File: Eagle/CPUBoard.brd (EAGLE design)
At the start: 100 x 80 mm, 33 parts, among them IC2 MAX232, IC3 MAX485CPA, J1 DISPLAY, J2 BUTTON_BOARD, J3 RELAY_BOARD, Q1 12.000MHz, X6 MKDSN1,5/3-5,08, X7 MKDSN1,5/3-5,08

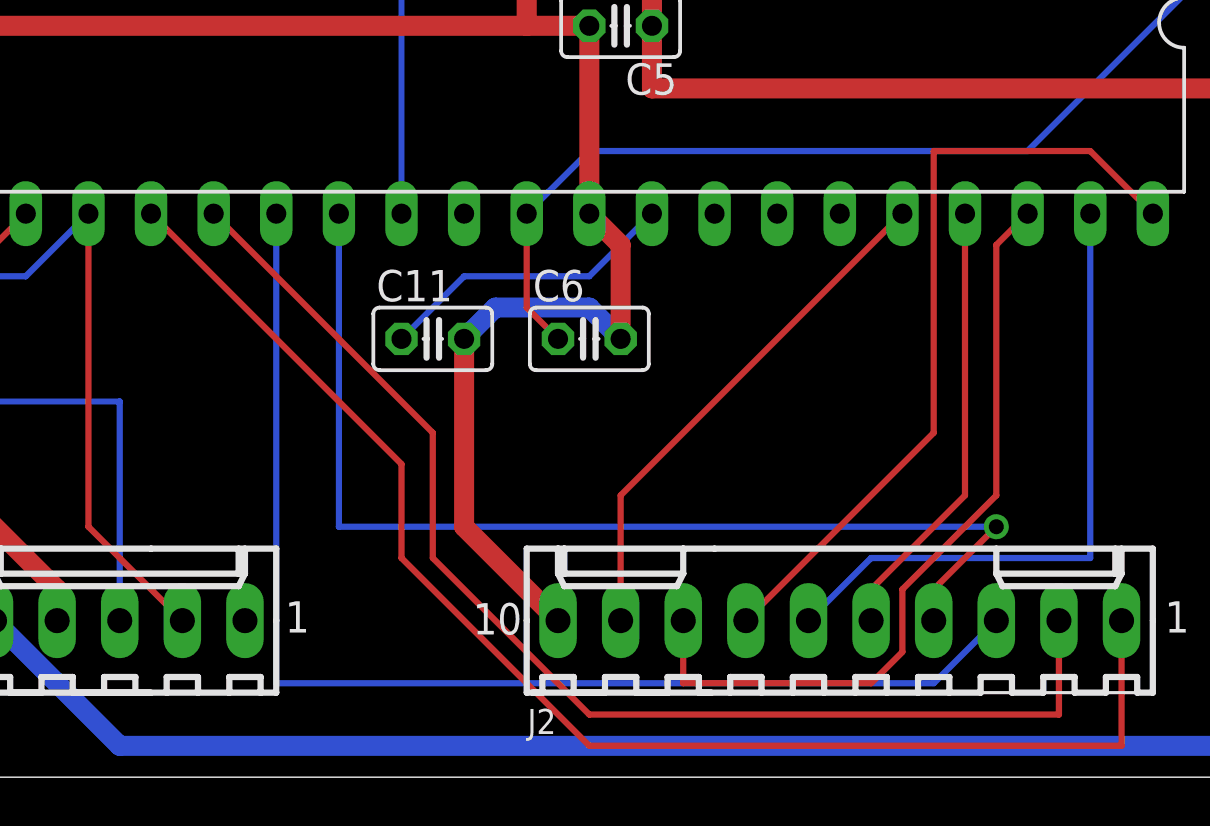
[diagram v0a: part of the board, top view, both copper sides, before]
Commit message: - cabling of RelayBoard1 partly changed - some pin-swaps to ButtonBoard -> blrtest.c finally works as expected
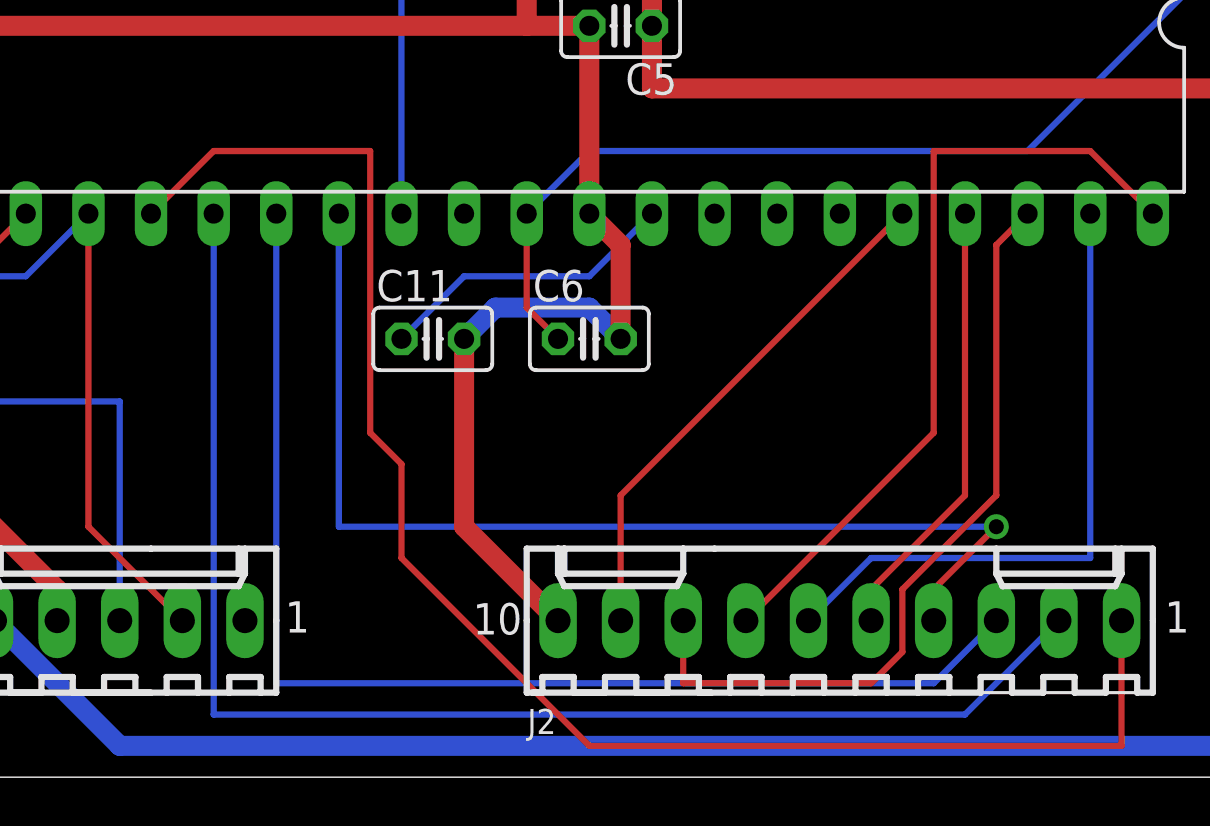
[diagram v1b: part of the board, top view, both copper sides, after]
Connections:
- removed net LED_GREEN: IC1.24, J2.1
- new net LED_RED: IC1.25, J2.2
- net LED_L: now also IC1.26, J2.3; no longer IC1.27, J2.4
- net LED_R: now also IC1.27, J2.4; no longer IC1.26, J2.3
- net LED_YELLOW: now also IC1.24, J2.1; no longer IC1.25, J2.2
- net LEFT: now also IC1.38, J2.8; no longer IC1.39, J2.6
- net PRESET_LEFT: now also IC1.36, J2.9; no longer IC1.37, J2.5
- net PRESET_RIGHT: now also IC1.37, J2.5; no longer IC1.36, J2.9
- net RIGHT: now also IC1.39, J2.6; no longer IC1.38, J2.8
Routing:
- net LED_RED: track 0.00 -> 56.2 mm
- net LED_GREEN: track 55.6 -> 0.00 mm
- net LED_YELLOW: track 49.5 -> 64.4 mm
- net RIGHT: track 31.8 -> 26.5 mm
- net LEFT: track 26.5 -> 31.8 mm
- net LED_R: track 49.3 -> 44.2 mm, vias 0 -> 1
- net LED_L: track 44.2 -> 49.3 mm, vias 1 -> 0
- net PRESET_RIGHT: track 21.2 -> 18.1 mm
- net PRESET_LEFT: track 18.1 -> 21.2 mm
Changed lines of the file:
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@@
 <wire x1="36.83" y1="73.66" x2="38.1" y2="74.93" width="0.254" layer="1"/>
 </signal>
-<signal name="LED_GREEN">
-<contactref element="IC1" pad="24"/>
-<contactref element="J2" pad="1"/>
-<wire x1="43.18" y1="12.7" x2="33.02" y2="22.86" width="0.254" layer="1"/>
-<wire x1="43.18" y1="8.89" x2="43.18" y2="12.7" width="0.254" layer="1"/>
-<wire x1="50.8" y1="1.27" x2="43.18" y2="8.89" width="0.254" layer="1"/>
-<wire x1="72.39" y1="1.27" x2="50.8" y2="1.27" width="0.254" layer="1"/>
-<wire x1="72.39" y1="6.35" x2="72.39" y2="1.27" width="0.254" layer="1"/>
-</signal>
-<signal name="LED_YELLOW">
-<contactref element="IC1" pad="25"/>
-<contactref element="J2" pad="2"/>
-<wire x1="44.45" y1="13.97" x2="35.56" y2="22.86" width="0.254" layer="1"/>
-<wire x1="44.45" y1="8.89" x2="44.45" y2="13.97" width="0.254" layer="1"/>
-<wire x1="50.8" y1="2.54" x2="44.45" y2="8.89" width="0.254" layer="1"/>
-<wire x1="69.85" y1="2.54" x2="50.8" y2="2.54" width="0.254" layer="1"/>
-<wire x1="69.85" y1="6.35" x2="69.85" y2="2.54" width="0.254" layer="1"/>
-</signal>
-<signal name="LED_L">
-<contactref element="IC1" pad="27"/>
-<contactref element="J2" pad="4"/>
-<wire x1="40.64" y1="10.16" x2="40.64" y2="22.86" width="0.254" layer="16"/>
-<wire x1="67.31" y1="10.16" x2="40.64" y2="10.16" width="0.254" layer="16"/>
-<wire x1="64.77" y1="7.62" x2="67.31" y2="10.16" width="0.254" layer="1"/>
-<wire x1="64.77" y1="6.35" x2="64.77" y2="7.62" width="0.254" layer="1"/>
-<via x="67.31" y="10.16" extent="1-16" drill="0.6096"/>
-</signal>
-<signal name="LED_R">
-<contactref element="IC1" pad="26"/>
-<contactref element="J2" pad="3"/>
-<wire x1="38.1" y1="3.81" x2="38.1" y2="22.86" width="0.254" layer="16"/>
-<wire x1="64.77" y1="3.81" x2="38.1" y2="3.81" width="0.254" layer="16"/>
-<wire x1="67.31" y1="6.35" x2="64.77" y2="3.81" width="0.254" layer="16"/>
-</signal>
-<signal name="PRESET_LEFT">
+<signal name="PRESET_RIGHT">
 <contactref element="IC1" pad="37"/>
 <contactref element="J2" pad="5"/>
@@
 <wire x1="62.23" y1="6.35" x2="62.23" y2="7.62" width="0.254" layer="1"/>
 </signal>
-<signal name="LEFT">
+<signal name="RIGHT">
 <contactref element="IC1" pad="39"/>
 <contactref element="J2" pad="6"/>
@@
 <wire x1="57.15" y1="6.35" x2="64.77" y2="13.97" width="0.254" layer="1"/>
 </signal>
-<signal name="RIGHT">
+<signal name="LEFT">
 <contactref element="IC1" pad="38"/>
 <contactref element="J2" pad="8"/>
@@
 <wire x1="54.61" y1="6.35" x2="54.61" y2="3.81" width="0.254" layer="1"/>
 </signal>
-<signal name="PRESET_RIGHT">
+<signal name="PRESET_LEFT">
 <contactref element="IC1" pad="36"/>
 <contactref element="J2" pad="9"/>
@@
 <wire x1="29.21" y1="58.42" x2="27.94" y2="58.42" width="0.254" layer="16"/>
 </signal>
+<signal name="LED_R">
+<contactref element="J2" pad="4"/>
+<contactref element="IC1" pad="27"/>
+<wire x1="40.64" y1="10.16" x2="40.64" y2="22.86" width="0.254" layer="16"/>
+<wire x1="67.31" y1="10.16" x2="40.64" y2="10.16" width="0.254" layer="16"/>
+<wire x1="64.77" y1="7.62" x2="67.31" y2="10.16" width="0.254" layer="1"/>
+<via x="67.31" y="10.16" extent="1-16" drill="0.6096"/>
+<wire x1="64.77" y1="7.62" x2="64.77" y2="6.35" width="0.254" layer="1"/>
+</signal>
+<signal name="LED_L">
+<contactref element="IC1" pad="26"/>
+<contactref element="J2" pad="3"/>
+<wire x1="64.77" y1="3.81" x2="38.1" y2="3.81" width="0.254" layer="16"/>
+<wire x1="67.31" y1="6.35" x2="64.77" y2="3.81" width="0.254" layer="16"/>
+<wire x1="38.1" y1="3.81" x2="38.1" y2="22.86" width="0.254" layer="16"/>
+</signal>
+<signal name="LED_RED">
+<contactref element="IC1" pad="25"/>
+<contactref element="J2" pad="2"/>
+<wire x1="35.56" y1="2.54" x2="35.56" y2="22.86" width="0.254" layer="16"/>
+<wire x1="66.04" y1="2.54" x2="35.56" y2="2.54" width="0.254" layer="16"/>
+<wire x1="69.85" y1="6.35" x2="66.04" y2="2.54" width="0.254" layer="16"/>
+</signal>
+<signal name="LED_YELLOW">
+<contactref element="IC1" pad="24"/>
+<contactref element="J2" pad="1"/>
+<wire x1="43.18" y1="8.89" x2="43.18" y2="12.7" width="0.254" layer="1"/>
+<wire x1="50.8" y1="1.27" x2="43.18" y2="8.89" width="0.254" layer="1"/>
+<wire x1="72.39" y1="1.27" x2="50.8" y2="1.27" width="0.254" layer="1"/>
+<wire x1="72.39" y1="6.35" x2="72.39" y2="1.27" width="0.254" layer="1"/>
+<wire x1="35.56" y1="25.4" x2="33.02" y2="22.86" width="0.254" layer="1"/>
+<wire x1="41.91" y1="25.4" x2="35.56" y2="25.4" width="0.254" layer="1"/>
+<wire x1="41.91" y1="13.97" x2="41.91" y2="25.4" width="0.254" layer="1"/>
+<wire x1="43.18" y1="12.7" x2="41.91" y2="13.97" width="0.254" layer="1"/>
+</signal>
 </signals>
